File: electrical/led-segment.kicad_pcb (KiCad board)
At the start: 4 copper layers, 65.2 x 95.7 mm, 32 parts

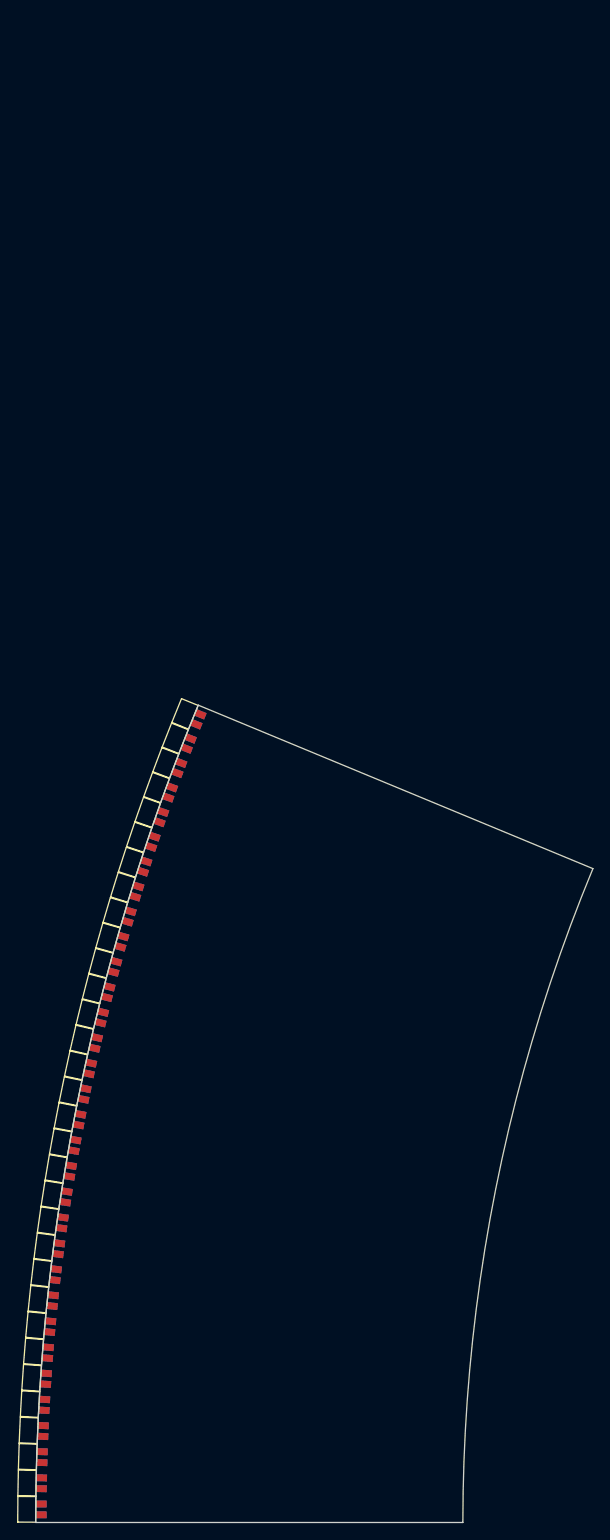
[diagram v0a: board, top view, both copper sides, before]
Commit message: Route led-segment board.
Should be complete now.
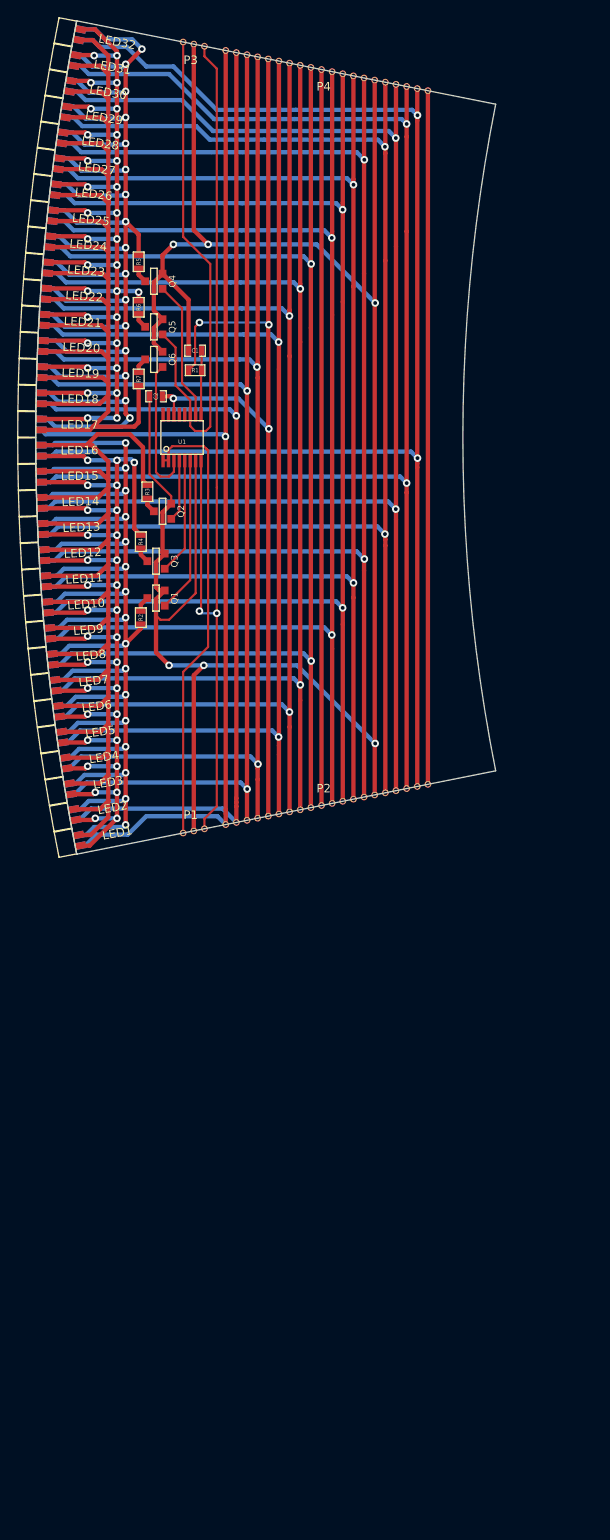
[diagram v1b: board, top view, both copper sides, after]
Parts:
- added C1: C, SM0603_Capa, F.Cu at (168.7, 116.8)
- added C2: C, SM0603_Capa, F.Cu at (164.1, 122.2)
- added P1: CONN_3, boardedge_3, F.Cu at (167.3, 173.3)
- added P2: CONN_20, boardedge_20, F.Cu at (172.2, 172.3)
- added P3: CONN_3, boardedge_3, F.Cu at (167.3, 80.7)
- added P4: CONN_20, boardedge_20, F.Cu at (172.2, 81.7)
- added Q1: FDV301N, SOT23GDS, F.Cu at (164.1, 145.8)
- added Q2: FDV301N, SOT23GDS, F.Cu at (164.8, 135.6)
- added Q3: FDV301N, SOT23GDS, F.Cu at (164.1, 141.5)
- added Q4: FDV301N, SOT23GDS, F.Cu at (163.8, 108.7)
- added Q5: FDV301N, SOT23GDS, F.Cu at (163.8, 114.0)
- added Q6: FDV301N, SOT23GDS, F.Cu at (163.8, 117.9)
- added R1: R, SM0603, F.Cu at (168.7, 119.1)
- added R2: R, SM0603, F.Cu at (162.3, 148.1)
- added R3: R, SM0603, F.Cu at (163.1, 133.3)
- added R4: R, SM0603, F.Cu at (162.3, 139.2)
- added R5: R, SM0603, F.Cu at (162.1, 106.4)
- added R6: R, SM0603, F.Cu at (162.1, 111.8)
- added R7: R, SM0603, F.Cu at (162.1, 120.1)
- added U1: 74164, ssop-16, F.Cu at (167.1, 127.0)
- LED1, LED10, LED11, LED12, LED13, LED14, LED15, LED16, LED17, LED18, LED19, LED2, LED20, LED21, LED22, LED23, LED24, LED25, LED26, LED27, LED28, LED29, LED3, LED30, LED31, LED32, LED4, LED5, LED6, LED7, LED8, LED9: value PLCC4 -> PLCC4RGBCT-CA
- moved LED32 81.2 mm to (154.5, 79.7), turned to 79.1016 degrees
- moved LED31 81.0 mm to (153.9, 82.7), turned to 79.8047 degrees
- moved LED30 80.7 mm to (153.4, 85.8), turned to 80.5078 degrees
- moved LED29 80.5 mm to (152.9, 88.8), turned to 81.2109 degrees
- moved LED28 80.2 mm to (152.5, 91.8), turned to 81.9141 degrees
- moved LED27 80.0 mm to (152.1, 94.9), turned to 82.6172 degrees
- moved LED26 79.8 mm to (151.7, 97.9), turned to 83.3203 degrees
- moved LED25 79.6 mm to (151.4, 101.0), turned to 84.0234 degrees
- moved LED24 79.4 mm to (151.1, 104.0), turned to 84.7266 degrees
- moved LED23 79.2 mm to (150.8, 107.1), turned to 85.4297 degrees
- moved LED22 79.1 mm to (150.6, 110.1), turned to 86.1328 degrees
- moved LED21 78.9 mm to (150.4, 113.2), turned to 86.8359 degrees
- moved LED20 78.8 mm to (150.2, 116.3), turned to 87.5391 degrees
- moved LED19 78.7 mm to (150.1, 119.3), turned to 88.2422 degrees
- moved LED18 78.5 mm to (150.0, 122.4), turned to 88.9453 degrees
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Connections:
- LED1 pad 1: (no net) -> /8xLED group A/LCR
- LED1 pad 2: (no net) -> /LRA0
- LED1 pad 3: (no net) -> /8xLED group A/LCB
- LED1 pad 4: (no net) -> /8xLED group A/LCG
- LED10 pad 1: (no net) -> /8xLED group A/LCR
- LED10 pad 2: (no net) -> /LRB1
- LED10 pad 3: (no net) -> /8xLED group A/LCB
- LED10 pad 4: (no net) -> /8xLED group A/LCG
- LED11 pad 1: (no net) -> /8xLED group A/LCR
- LED11 pad 2: (no net) -> /LRB2
- LED11 pad 3: (no net) -> /8xLED group A/LCB
- LED11 pad 4: (no net) -> /8xLED group A/LCG
- LED12 pad 1: (no net) -> /8xLED group A/LCR
- LED12 pad 2: (no net) -> /LRB3
- LED12 pad 3: (no net) -> /8xLED group A/LCB
- LED12 pad 4: (no net) -> /8xLED group A/LCG
- LED13 pad 1: (no net) -> /8xLED group A/LCR
- LED13 pad 2: (no net) -> /LRB4
- LED13 pad 3: (no net) -> /8xLED group A/LCB
- LED13 pad 4: (no net) -> /8xLED group A/LCG
- LED14 pad 1: (no net) -> /8xLED group A/LCR
- LED14 pad 2: (no net) -> /LRB5
- LED14 pad 3: (no net) -> /8xLED group A/LCB
- LED14 pad 4: (no net) -> /8xLED group A/LCG
- LED15 pad 1: (no net) -> /8xLED group A/LCR
- LED15 pad 2: (no net) -> /LRB6
- LED15 pad 3: (no net) -> /8xLED group A/LCB
- LED15 pad 4: (no net) -> /8xLED group A/LCG
- LED16 pad 1: (no net) -> /8xLED group A/LCR
- LED16 pad 2: (no net) -> /LRB7
- LED16 pad 3: (no net) -> /8xLED group A/LCB
- LED16 pad 4: (no net) -> /8xLED group A/LCG
- LED17 pad 1: (no net) -> /8xLED group C/LCR
- LED17 pad 2: (no net) -> /LRA0
- LED17 pad 3: (no net) -> /8xLED group C/LCB
- LED17 pad 4: (no net) -> /8xLED group C/LCG
- LED18 pad 1: (no net) -> /8xLED group C/LCR
- LED18 pad 2: (no net) -> /LRA1
- LED18 pad 3: (no net) -> /8xLED group C/LCB
- LED18 pad 4: (no net) -> /8xLED group C/LCG
- LED19 pad 1: (no net) -> /8xLED group C/LCR
- LED19 pad 2: (no net) -> /LRA2
- LED19 pad 3: (no net) -> /8xLED group C/LCB
- LED19 pad 4: (no net) -> /8xLED group C/LCG
- LED2 pad 1: (no net) -> /8xLED group A/LCR
- LED2 pad 2: (no net) -> /LRA1
- LED2 pad 3: (no net) -> /8xLED group A/LCB
- LED2 pad 4: (no net) -> /8xLED group A/LCG
- LED20 pad 1: (no net) -> /8xLED group C/LCR
- LED20 pad 2: (no net) -> /LRA3
- LED20 pad 3: (no net) -> /8xLED group C/LCB
- LED20 pad 4: (no net) -> /8xLED group C/LCG
- LED21 pad 1: (no net) -> /8xLED group C/LCR
- LED21 pad 2: (no net) -> /LRA4
- LED21 pad 3: (no net) -> /8xLED group C/LCB
- LED21 pad 4: (no net) -> /8xLED group C/LCG
- LED22 pad 1: (no net) -> /8xLED group C/LCR
- LED22 pad 2: (no net) -> /LRA5
- LED22 pad 3: (no net) -> /8xLED group C/LCB
- LED22 pad 4: (no net) -> /8xLED group C/LCG
- LED23 pad 1: (no net) -> /8xLED group C/LCR
- LED23 pad 2: (no net) -> /LRA6
- LED23 pad 3: (no net) -> /8xLED group C/LCB
- LED23 pad 4: (no net) -> /8xLED group C/LCG
- LED24 pad 1: (no net) -> /8xLED group C/LCR
- LED24 pad 2: (no net) -> /LRA7
- LED24 pad 3: (no net) -> /8xLED group C/LCB
- LED24 pad 4: (no net) -> /8xLED group C/LCG
- LED25 pad 1: (no net) -> /8xLED group C/LCR
- LED25 pad 2: (no net) -> /LRB0
- LED25 pad 3: (no net) -> /8xLED group C/LCB
- LED25 pad 4: (no net) -> /8xLED group C/LCG
- LED26 pad 1: (no net) -> /8xLED group C/LCR
- LED26 pad 2: (no net) -> /LRB1
- LED26 pad 3: (no net) -> /8xLED group C/LCB
- LED26 pad 4: (no net) -> /8xLED group C/LCG
- LED27 pad 1: (no net) -> /8xLED group C/LCR
- LED27 pad 2: (no net) -> /LRB2
- LED27 pad 3: (no net) -> /8xLED group C/LCB
- LED27 pad 4: (no net) -> /8xLED group C/LCG
- LED28 pad 1: (no net) -> /8xLED group C/LCR
- LED28 pad 2: (no net) -> /LRB3
- LED28 pad 3: (no net) -> /8xLED group C/LCB
- LED28 pad 4: (no net) -> /8xLED group C/LCG
- LED29 pad 1: (no net) -> /8xLED group C/LCR
- LED29 pad 2: (no net) -> /LRB4
- LED29 pad 3: (no net) -> /8xLED group C/LCB
- LED29 pad 4: (no net) -> /8xLED group C/LCG
- LED3 pad 1: (no net) -> /8xLED group A/LCR
- LED3 pad 2: (no net) -> /LRA2
- LED3 pad 3: (no net) -> /8xLED group A/LCB
- LED3 pad 4: (no net) -> /8xLED group A/LCG
- LED30 pad 1: (no net) -> /8xLED group C/LCR
- LED30 pad 2: (no net) -> /LRB5
- LED30 pad 3: (no net) -> /8xLED group C/LCB
- LED30 pad 4: (no net) -> /8xLED group C/LCG
- LED31 pad 1: (no net) -> /8xLED group C/LCR
- LED31 pad 2: (no net) -> /LRB6
- LED31 pad 3: (no net) -> /8xLED group C/LCB
- LED31 pad 4: (no net) -> /8xLED group C/LCG
- LED32 pad 1: (no net) -> /8xLED group C/LCR
- LED32 pad 2: (no net) -> /LRB7
- LED32 pad 3: (no net) -> /8xLED group C/LCB
- LED32 pad 4: (no net) -> /8xLED group C/LCG
- LED4 pad 1: (no net) -> /8xLED group A/LCR
- LED4 pad 2: (no net) -> /LRA3
- LED4 pad 3: (no net) -> /8xLED group A/LCB
- LED4 pad 4: (no net) -> /8xLED group A/LCG
- LED5 pad 1: (no net) -> /8xLED group A/LCR
- LED5 pad 2: (no net) -> /LRA4
- LED5 pad 3: (no net) -> /8xLED group A/LCB
- LED5 pad 4: (no net) -> /8xLED group A/LCG
- LED6 pad 1: (no net) -> /8xLED group A/LCR
- LED6 pad 2: (no net) -> /LRA5
- LED6 pad 3: (no net) -> /8xLED group A/LCB
- LED6 pad 4: (no net) -> /8xLED group A/LCG
- LED7 pad 1: (no net) -> /8xLED group A/LCR
- LED7 pad 2: (no net) -> /LRA6
- LED7 pad 3: (no net) -> /8xLED group A/LCB
- LED7 pad 4: (no net) -> /8xLED group A/LCG
- LED8 pad 1: (no net) -> /8xLED group A/LCR
- LED8 pad 2: (no net) -> /LRA7
- LED8 pad 3: (no net) -> /8xLED group A/LCB
- LED8 pad 4: (no net) -> /8xLED group A/LCG
- LED9 pad 1: (no net) -> /8xLED group A/LCR
- LED9 pad 2: (no net) -> /LRB0
- LED9 pad 3: (no net) -> /8xLED group A/LCB
- LED9 pad 4: (no net) -> /8xLED group A/LCG
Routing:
- net GND: track 0.00 -> 348.9 mm, vias 0 -> 6
- net +5V: track 0.00 -> 205.2 mm, vias 0 -> 4
- net /8xLED group C/LCB: track 0.00 -> 194.3 mm, vias 0 -> 16
- net /8xLED group A/LCB: track 0.00 -> 188.6 mm, vias 0 -> 16
- net /8xLED group A/LCR: track 0.00 -> 171.7 mm, vias 0 -> 31
- net /LRB7: track 0.00 -> 169.8 mm, vias 0 -> 2
- net /LRB6: track 0.00 -> 167.6 mm, vias 0 -> 2
- net /LRB5: track 0.00 -> 165.4 mm, vias 0 -> 2
- net /8xLED group C/LCG: track 0.00 -> 164.5 mm, vias 0 -> 31
- net /8xLED group A/LCG: track 0.00 -> 163.3 mm
- net /LRB4: track 0.00 -> 163.0 mm, vias 0 -> 2
- net /8xLED group C/LCR: track 0.00 -> 159.3 mm
- net /LRB3: track 0.00 -> 158.9 mm, vias 0 -> 2
- net /LRB2: track 0.00 -> 156.8 mm, vias 0 -> 2
- net /LRB1: track 0.00 -> 154.9 mm, vias 0 -> 2
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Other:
- board size 65.2 x 95.7 mm -> 53.8 x 97.5 mm
- net class Default: trace_width 0.254 -> 0.508
- net class signal added: clearance 0.254, trace_width 0.254, via_dia 0.889, via_drill 0.635

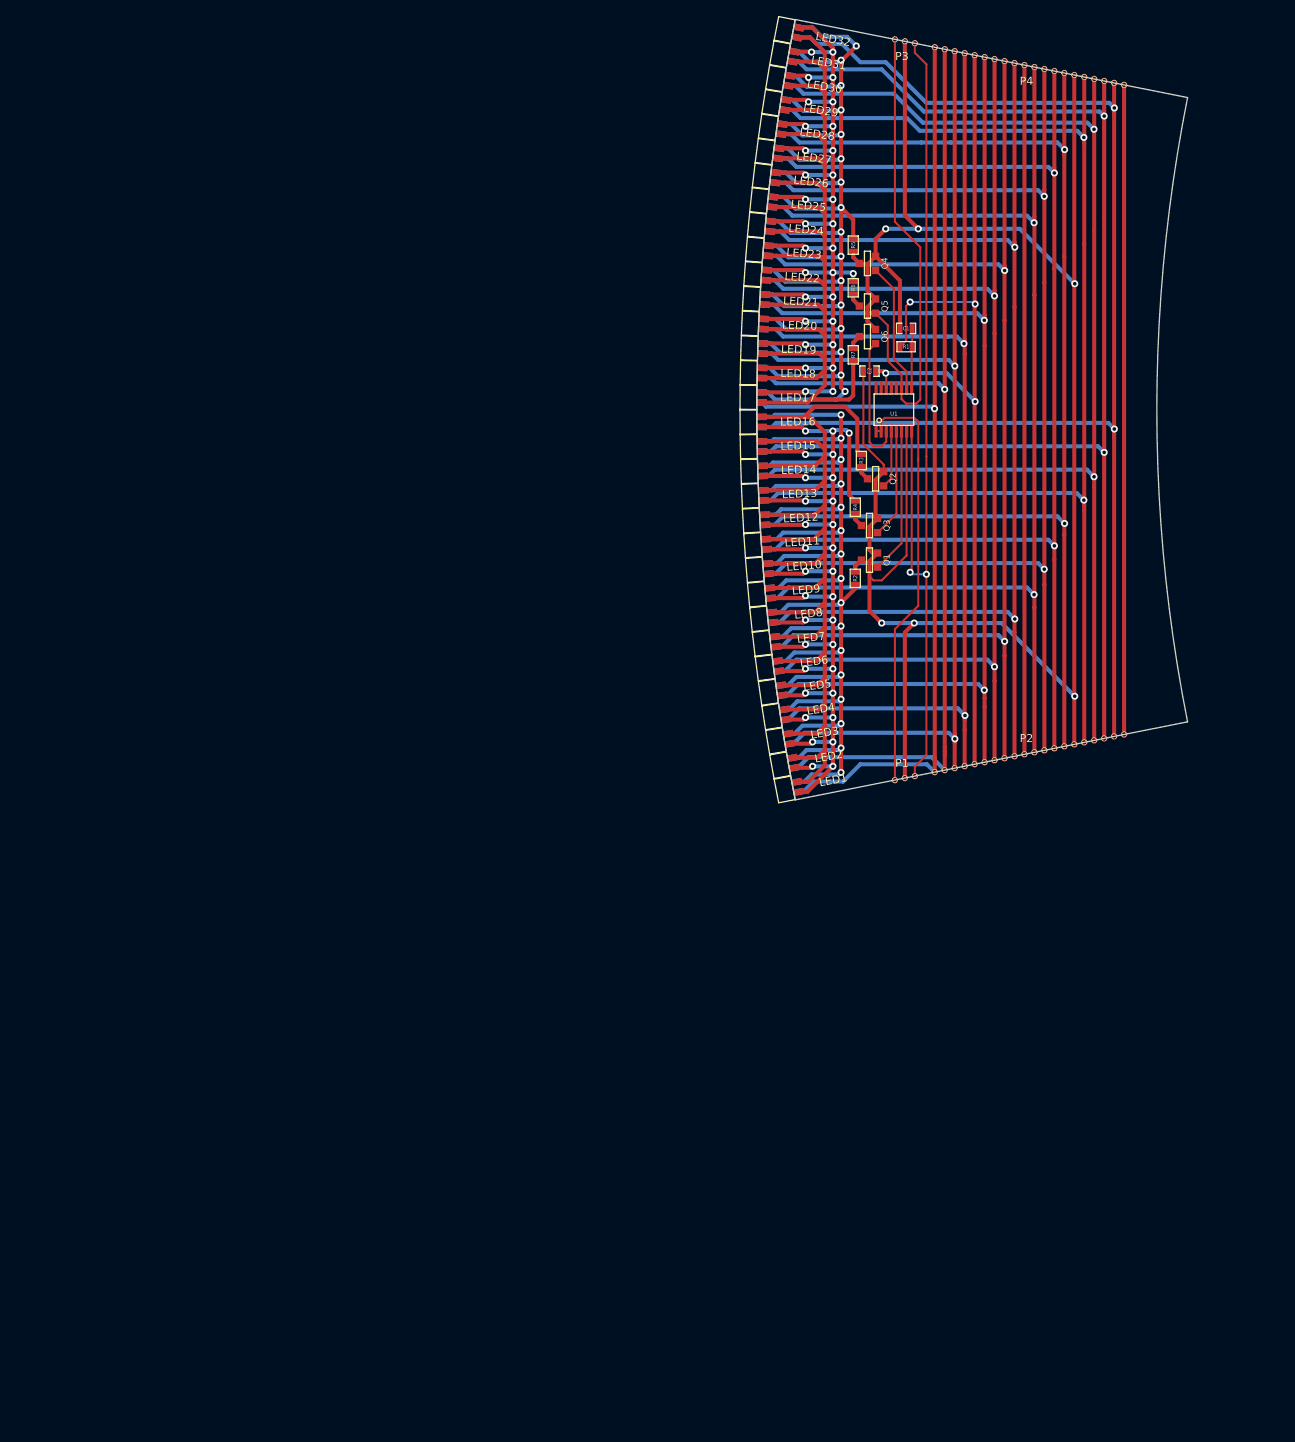
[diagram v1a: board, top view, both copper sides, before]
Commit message: Change led-segments PCB to A4.
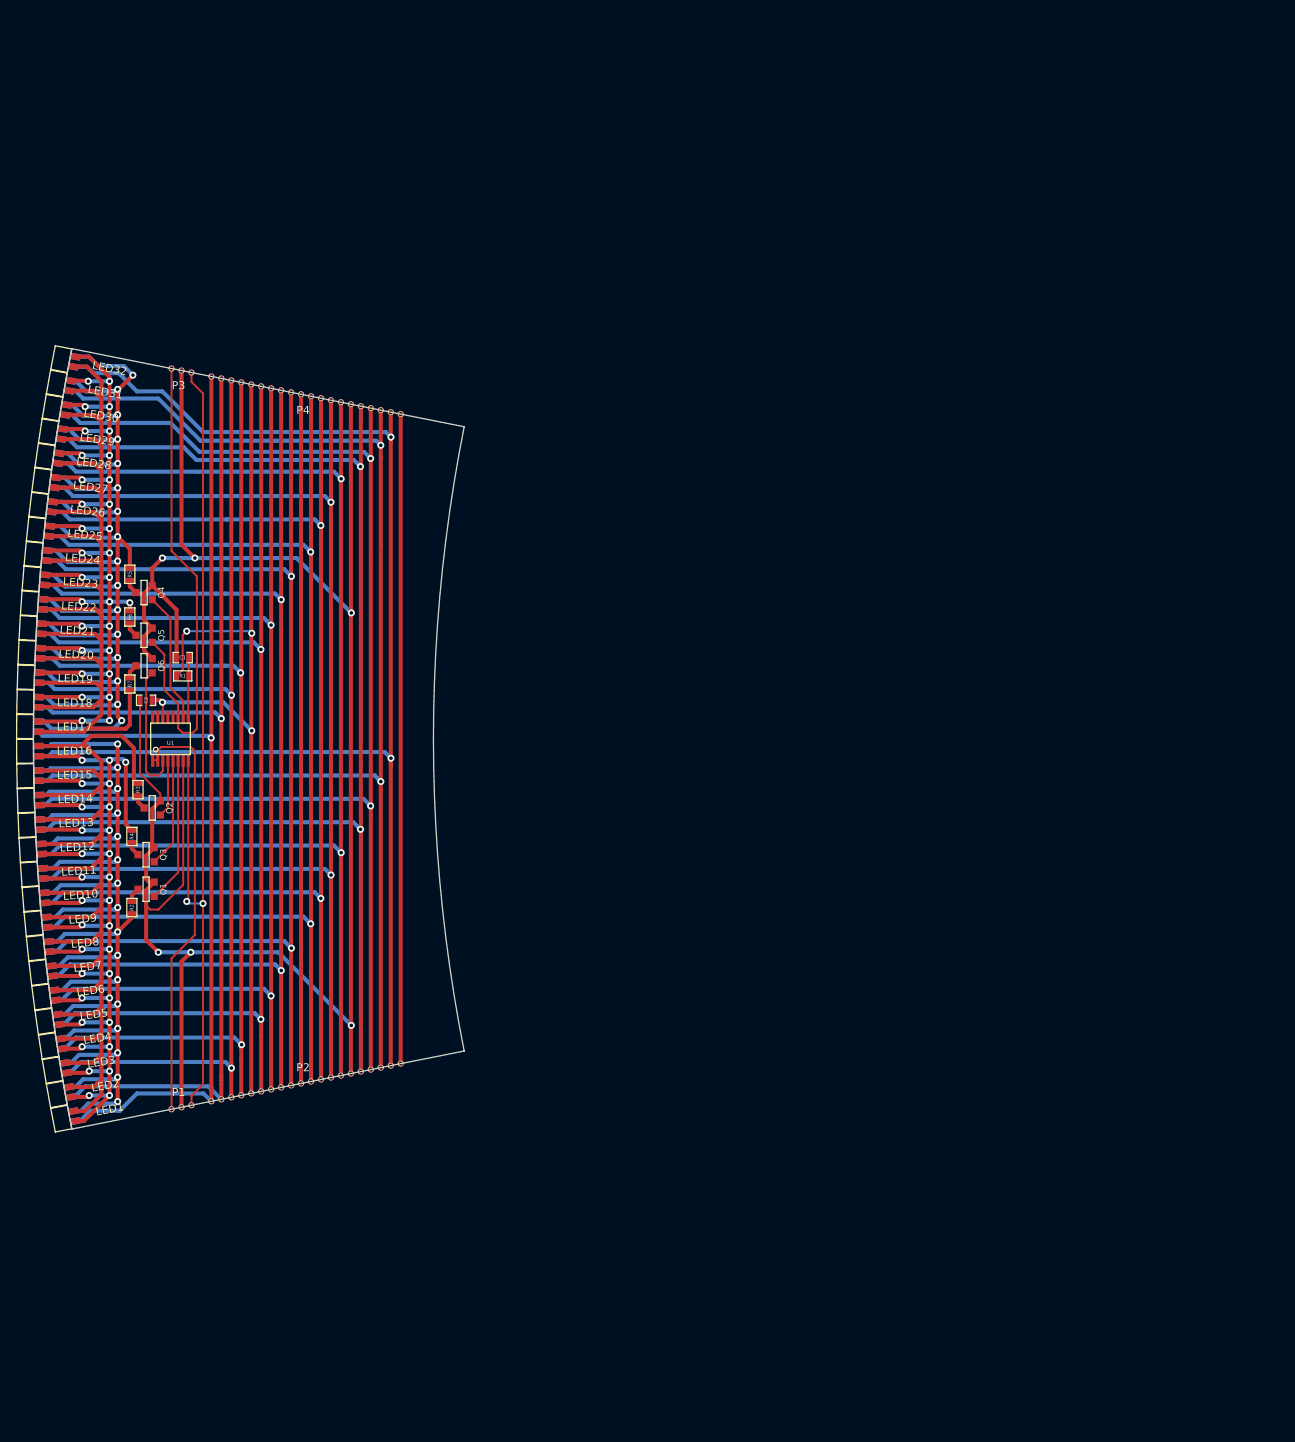
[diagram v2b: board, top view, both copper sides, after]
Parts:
- moved C1 99.3 mm to (78.2, 158.0)
- moved C2 99.3 mm to (73.7, 163.3)
- moved LED10 99.3 mm to (60.4, 188.1)
- moved LED11 99.3 mm to (60.1, 185.0)
- moved LED13 99.3 mm to (59.8, 178.9)
- moved LED14 99.3 mm to (59.7, 175.8)
- moved LED16 99.3 mm to (59.6, 169.7)
- moved LED19 99.3 mm to (59.7, 160.5)
- moved LED20 99.3 mm to (59.8, 157.4)
- moved LED22 99.3 mm to (60.1, 151.3)
- moved LED23 99.3 mm to (60.4, 148.2)
- moved LED25 99.3 mm to (60.9, 142.1)
- moved LED26 99.3 mm to (61.3, 139.1)
- moved LED27 99.3 mm to (61.6, 136.0)
- moved LED29 99.3 mm to (62.5, 129.9)
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
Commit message: Enlarge boardedge pads. Small track fixups.
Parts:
- turned P1 to 11.2 degrees
- turned P2 to 11.2 degrees
- turned P3 to 348.7 degrees
- turned P4 to 348.7 degrees
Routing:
- net +5V: track 205.2 -> 211.5 mm, vias 4 -> 5
- net GND: track 348.9 -> 355.1 mm, vias 6 -> 7
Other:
- outline, holes or cut-outs redrawn

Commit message: Add led-segment ground plane. Convert to two layer.
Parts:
- moved C1 2.29 mm to (78.2, 160.3)
- moved R1 2.29 mm to (78.2, 158.0)
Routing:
- net GND: track 355.1 -> 260.2 mm, vias 7 -> 4
- net +5V: track 211.5 -> 209.3 mm
- added copper zone on B.Cu, net GND
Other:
- outline, holes or cut-outs redrawn
- copper layers 4 -> 2
- net class Default: clearance 0.254 -> 0.2286
- net class signal: clearance 0.254 -> 0.2286
- rule trace_clearance: 0.254 -> 0.2286
- board text added: "pov-globe led-segment v1"
- board text added: "© 2014 makers-ie"
